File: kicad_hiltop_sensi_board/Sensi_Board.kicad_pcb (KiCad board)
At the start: 4 copper layers, 159.9 x 99.9 mm, 418 parts, among them J1 Conn_02x06_Counter_Clockwise, J10 Conn_ARM_JTAG_SWD_10, J2 Conn_02x06_Counter_Clockwise, J3 Conn_03x32_DIN41612, J4 Conn_02x06_Counter_Clockwise, J5 Conn_02x06_Counter_Clockwise, J6 Conn_02x06_Counter_Clockwise, J7 Conn_02x06_Counter_Clockwise, J8 Conn_02x06_Counter_Clockwise, K1 HRS1KH-S, Q10 ZXMN6A07F, Q11 ZXMN6A07F, Q2 ZXMN6A07F, Q7 ZXMN6A07F, Q8 ZXMN6A07F, SW1 SW_Push, SW2 SW_DIP_x04, SW3 SW_DIP_x04, SW4 SW_DIP_x04, SW5 SW_DIP_x04, U1 INA250A4, U10 MAX31865, U11 MAX31865, U13 CP2102N-A01-GQFN24, U14 BTS4140N, U15 BTS4140N, U16 MAX4194, U17 BTS4140N, U18 BTS4140N, U19 MAX4194, U2 LD1117S33TR_SOT223, U20 MAX4194, U21 MAX4194, U22 STM32F072RBTx, U23 MAX4194, U24 MAX4194, U25 MAX4194, U26 MAX4194, U27 USB2502, U3 AT25DN512CSSHF-B, U4 AD8646, U5 AD8646, U6 LM75B, U7 AT24C02C-SSHM-T, U8 MAX31865, U9 MAX31865, Y1 50ppm 24.000MHZ, Y2 8MHZ, Y3 ABS25-32.768KHZ-6-T

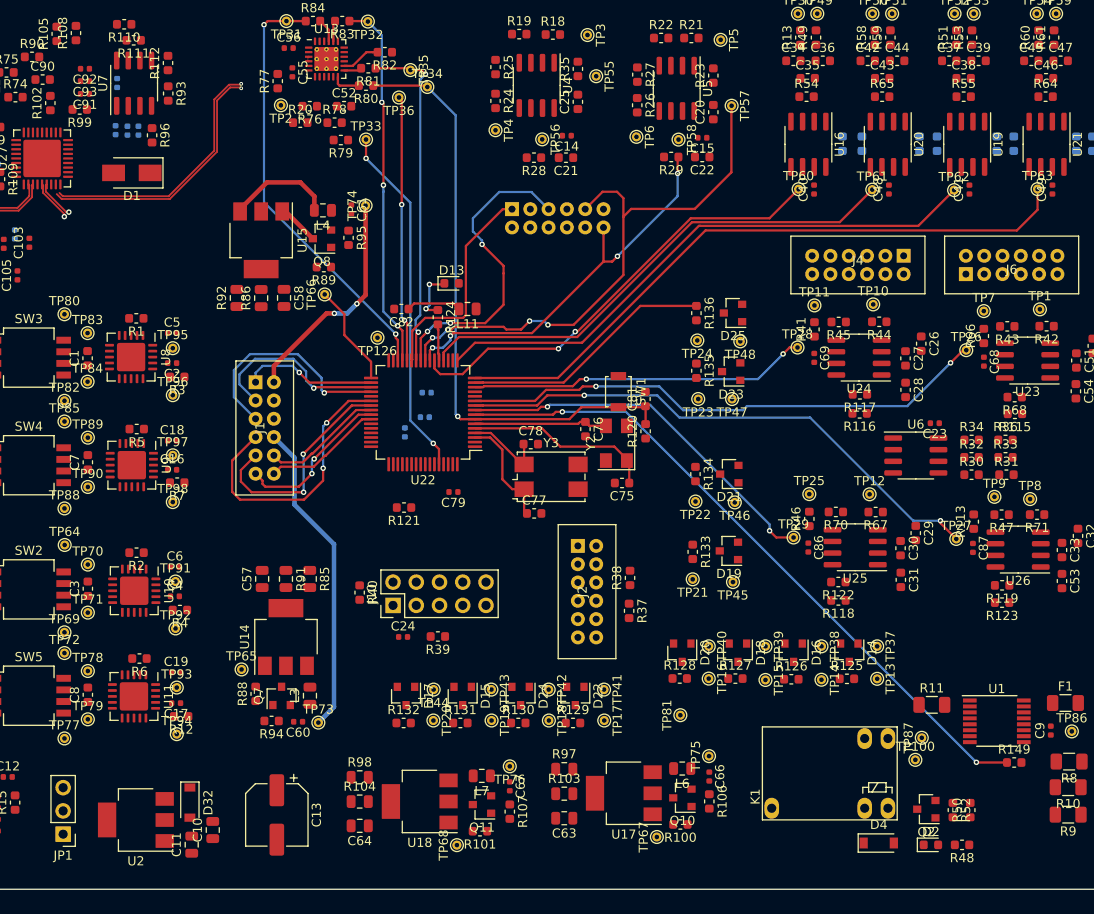
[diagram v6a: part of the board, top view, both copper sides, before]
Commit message: Routing complete around the chip of sensi board
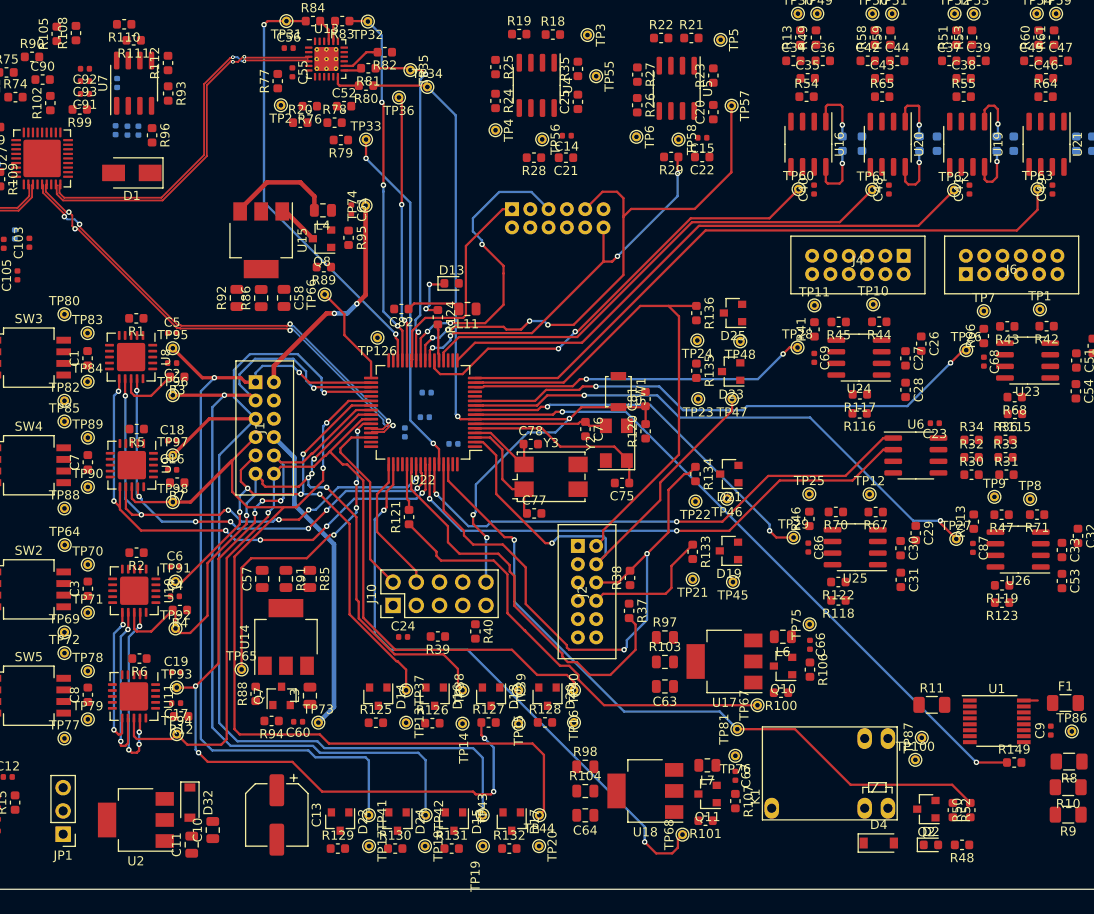
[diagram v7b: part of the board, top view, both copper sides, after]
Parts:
- C79: moved to B.Cu
- moved D14 51.7 mm to (120.4, 123.9)
- moved R125 51.7 mm to (120.1, 126.7)
- moved TP13 51.7 mm to (123.4, 126.7)
- moved TP37 51.7 mm to (123.4, 123.2)
- moved D16 39.5 mm to (126.6, 123.9)
- moved R126 39.5 mm to (126.3, 126.8)
- moved TP14 39.5 mm to (129.6, 126.8)
- moved TP38 39.5 mm to (129.6, 123.2)
- moved TP17 29.1 mm to (119.4, 140.2)
- moved TP41 29.1 mm to (119.4, 136.8)
- moved D22 29.1 mm to (116.2, 137.5)
- moved R129 29.1 mm to (116.0, 140.5)
- moved D18 27.4 mm to (132.7, 123.9)
- moved R127 27.4 mm to (132.4, 126.7)
- moved TP15 27.4 mm to (135.7, 126.8)
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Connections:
- J6 pad 4: /F2+ -> /F4+
- J6 pad 5: /F2- -> /F4-
- J6 pad 7: /F4- -> /F2-
- J6 pad 8: /F4+ -> /F2+
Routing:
- net /GPIO4: track 13.1 -> 104.2 mm, vias 0 -> 1
- net /GPIO6: track 20.6 -> 104.3 mm, vias 1 -> 2
- net /GPIO8: track 30.5 -> 113.6 mm
- net /GPIO3: track 13.3 -> 96.0 mm, vias 0 -> 7
- net /GPIO7: track 24.6 -> 106.8 mm
- net /RL1_OUT: track 0.00 -> 77.4 mm, vias 0 -> 1
- net /GPIO5: track 14.7 -> 90.7 mm, vias 1 -> 2
- net /STM_SPI1_MOSI: track 0.00 -> 72.9 mm, vias 0 -> 8
- net /STM_SPI1_SCK: track 0.00 -> 72.8 mm, vias 0 -> 8
- net /STM_SPI1_MISO: track 0.00 -> 71.3 mm, vias 0 -> 11
- net /GPIO2: track 17.5 -> 83.2 mm, vias 2 -> 5
- net /HS_CTRL_SW4: track 0.00 -> 65.3 mm, vias 0 -> 2
- net /GPIO10: track 0.00 -> 64.2 mm, vias 0 -> 2
- net /STM_SCL: track 0.00 -> 59.6 mm, vias 0 -> 2
- net /STM_SDA: track 0.00 -> 58.7 mm, vias 0 -> 2
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
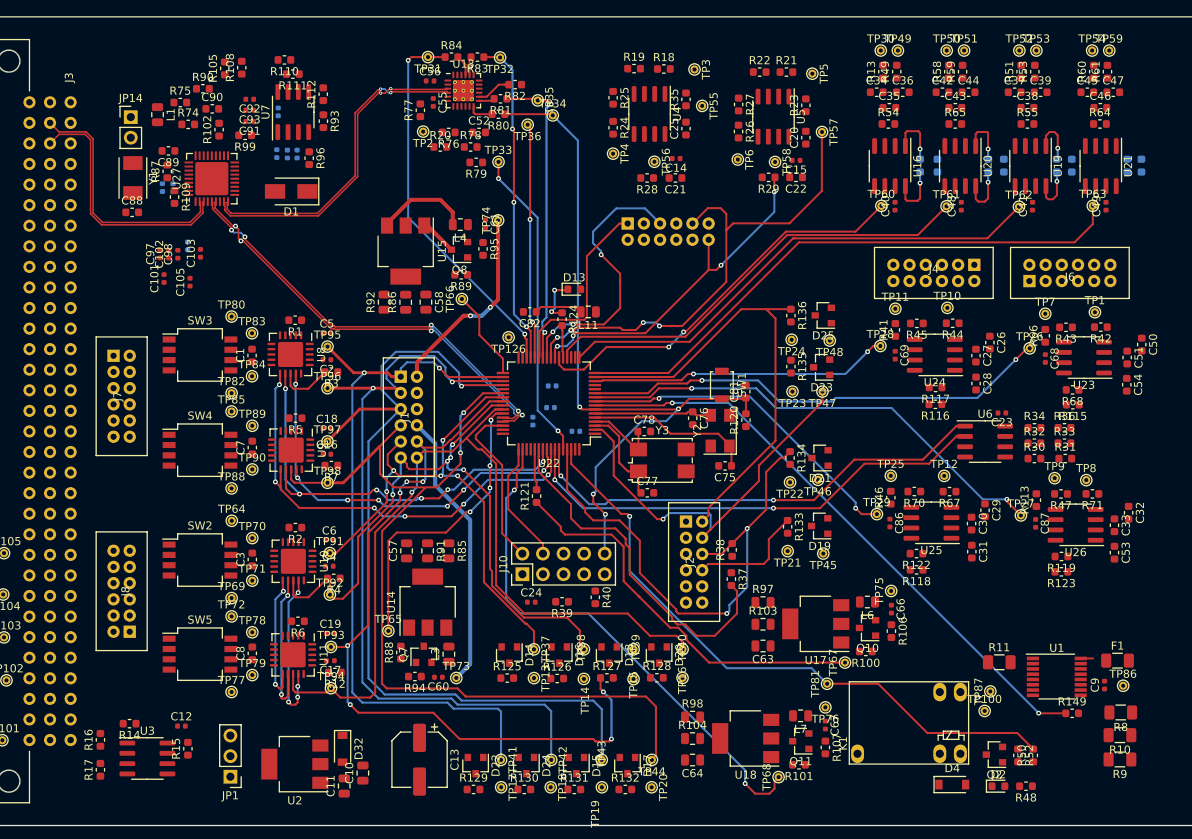
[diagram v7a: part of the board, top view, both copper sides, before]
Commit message: Most of the routing of the sensi board complete
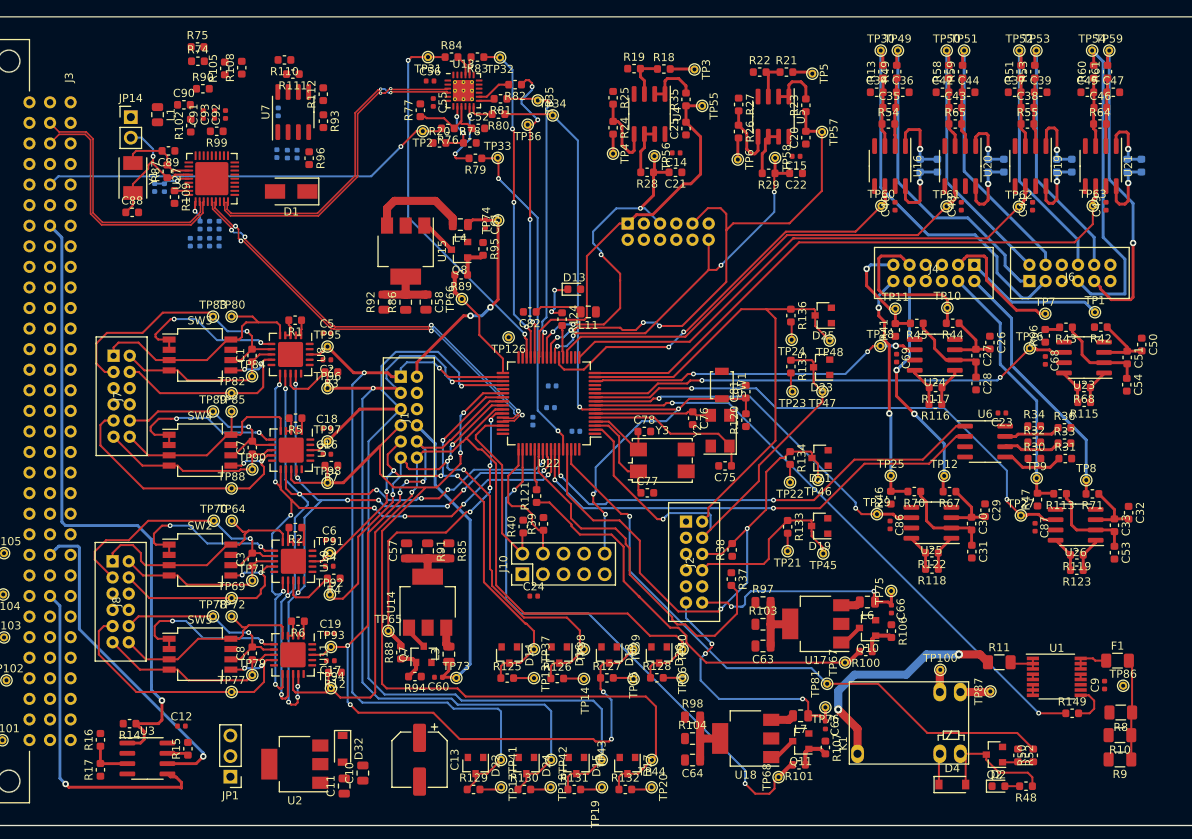
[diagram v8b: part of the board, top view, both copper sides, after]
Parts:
- C101, C102, C103, C105, C97, C98: moved to B.Cu
- moved R40 12.5 mm to (122.1, 108.0), turned to 90 degrees
- moved R39 9.88 mm to (124.6, 107.7), turned to 90 degrees
- moved C101 9.46 mm to (84.5, 70.8), turned to 270 degrees
- moved R74 7.89 mm to (81.9, 50.6)
- moved TP100 7.47 mm to (173.6, 125.7)
- moved C97 7.44 mm to (84.5, 72.9)
- moved R75 7.18 mm to (81.9, 48.8)
- moved C105 7.15 mm to (82.2, 70.8), turned to 270 degrees
- moved C91 5.81 mm to (82.6, 57.1), turned to 90 degrees
- moved C102 5.24 mm to (83.4, 72.9)
- moved TP83 5.24 mm to (83.8, 82.1)
- moved TP78 5.23 mm to (83.8, 119.1)
- moved TP70 5.21 mm to (83.9, 107.3)
- moved TP89 5.16 mm to (83.8, 93.8)
- moved C93 4.38 mm to (84.0, 57.1), turned to 90 degrees
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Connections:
- J4 pad 10: /TH3- -> GND
- J4 pad 11: /TH3+ -> /TH4+
- J4 pad 12: GND -> /TH4-
- J4 pad 4: /TH2+ -> GND
- J4 pad 5: /TH2- -> /TH3+
- J4 pad 6: GND -> /TH3-
- J4 pad 7: /TH4- -> /TH2+
- J4 pad 8: /TH4+ -> /TH2-
- J6 pad 1: /F1+ -> /F1-
- J6 pad 10: /F3- -> /F3+
- J6 pad 11: /F3+ -> /F3-
- J6 pad 2: /F1- -> /F1+
- J6 pad 7: /F2- -> /F2+
- J6 pad 8: /F2+ -> /F2-
- J7 pad 10: /RTD4_R- -> (no net)
- J7 pad 11: GND -> /RTD4_R+
- J7 pad 12: (no net) -> /RTD4_F+
- J7 pad 2: /RTD3_F- -> /RTD3_R+
- J7 pad 3: /RTD3_R+ -> (no net)
- J7 pad 4: /RTD3_R- -> GND
- J7 pad 5: GND -> /RTD4_F-
- J7 pad 6: (no net) -> /RTD4_R-
- J7 pad 7: /RTD4_F+ -> /RTD3_R-
- J7 pad 8: /RTD4_F- -> /RTD3_F-
- J7 pad 9: /RTD4_R+ -> GND
- J8 pad 10: /RTD2_R- -> (no net)
- J8 pad 11: GND -> /RTD2_R+
- J8 pad 12: (no net) -> /RTD2_F+
- J8 pad 2: /RTD1_F- -> /RTD1_R+
- J8 pad 3: /RTD1_R+ -> (no net)
- J8 pad 4: /RTD1_R- -> GND
- J8 pad 5: GND -> /RTD2_F-
- J8 pad 6: (no net) -> /RTD2_R-
- J8 pad 7: /RTD2_F+ -> /RTD1_R-
- J8 pad 8: /RTD2_F- -> /RTD1_F-
- J8 pad 9: /RTD2_R+ -> GND
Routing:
- net /PORT_SEL: track 0.00 -> 80.0 mm, vias 0 -> 1
- net /RESET: track 0.00 -> 51.2 mm, vias 0 -> 1
- net /F1+: track 0.00 -> 46.9 mm
- net /SPI0_MOSI: track 0.00 -> 41.4 mm, vias 0 -> 1
- net /SPI0_CLK: track 0.00 -> 41.1 mm, vias 0 -> 1
- net /F1-: track 0.00 -> 40.2 mm
- net /F4+: track 0.00 -> 40.1 mm
- net /F4-: track 0.00 -> 39.6 mm, vias 0 -> 1
- net /RTD2_F-: track 0.00 -> 35.8 mm, vias 0 -> 2
- net /RTD4_F-: track 0.00 -> 34.8 mm, vias 0 -> 2
- net /RTD3_R+: track 0.00 -> 34.2 mm, vias 0 -> 1
- net /RTD1_R+: track 0.00 -> 33.8 mm, vias 0 -> 1
- net /F2+: track 0.00 -> 32.6 mm
- net /F2-: track 0.00 -> 32.5 mm
- net /TH2-: track 0.00 -> 32.3 mm
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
